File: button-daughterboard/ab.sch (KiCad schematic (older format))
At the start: 9 parts, among them J6 Conn_01x01, J7 Conn_01x01, J8 Conn_01x01, SW5 SW_Push, SW6 SW_Push

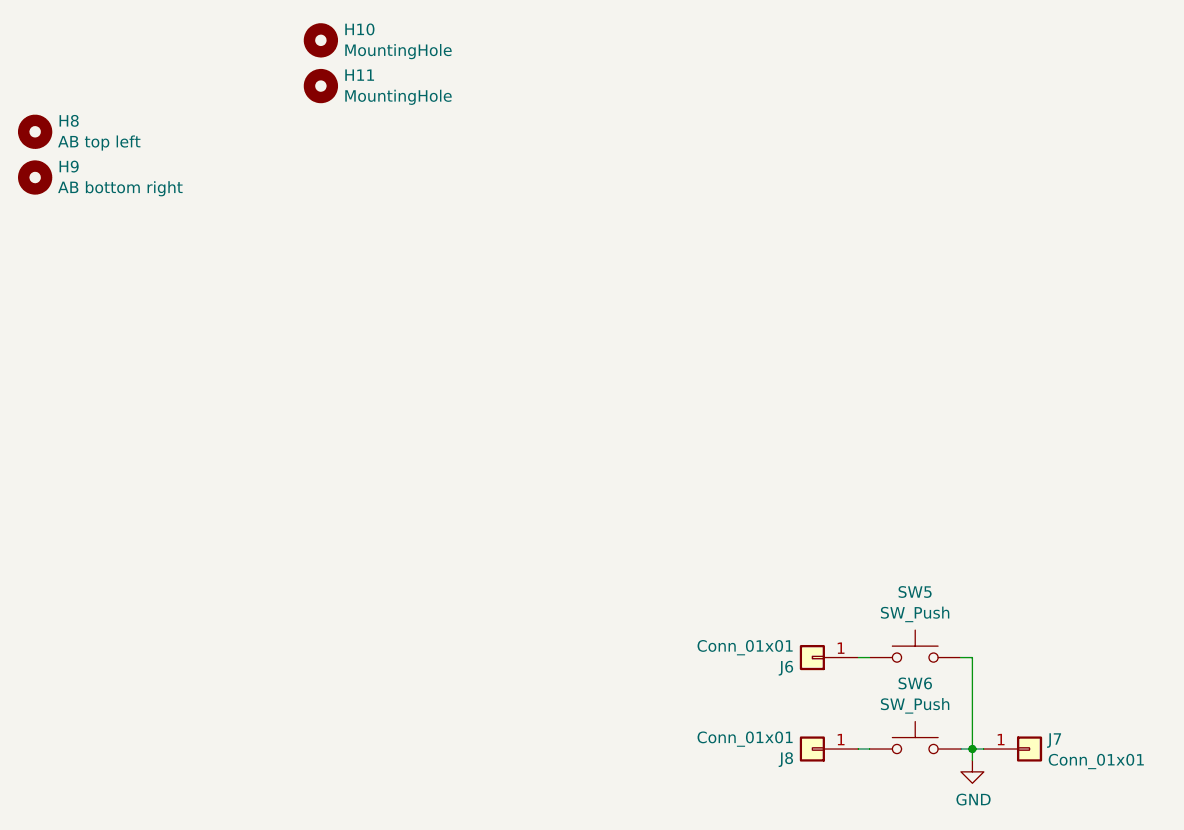
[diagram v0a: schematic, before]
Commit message: Panelize button daughterboards
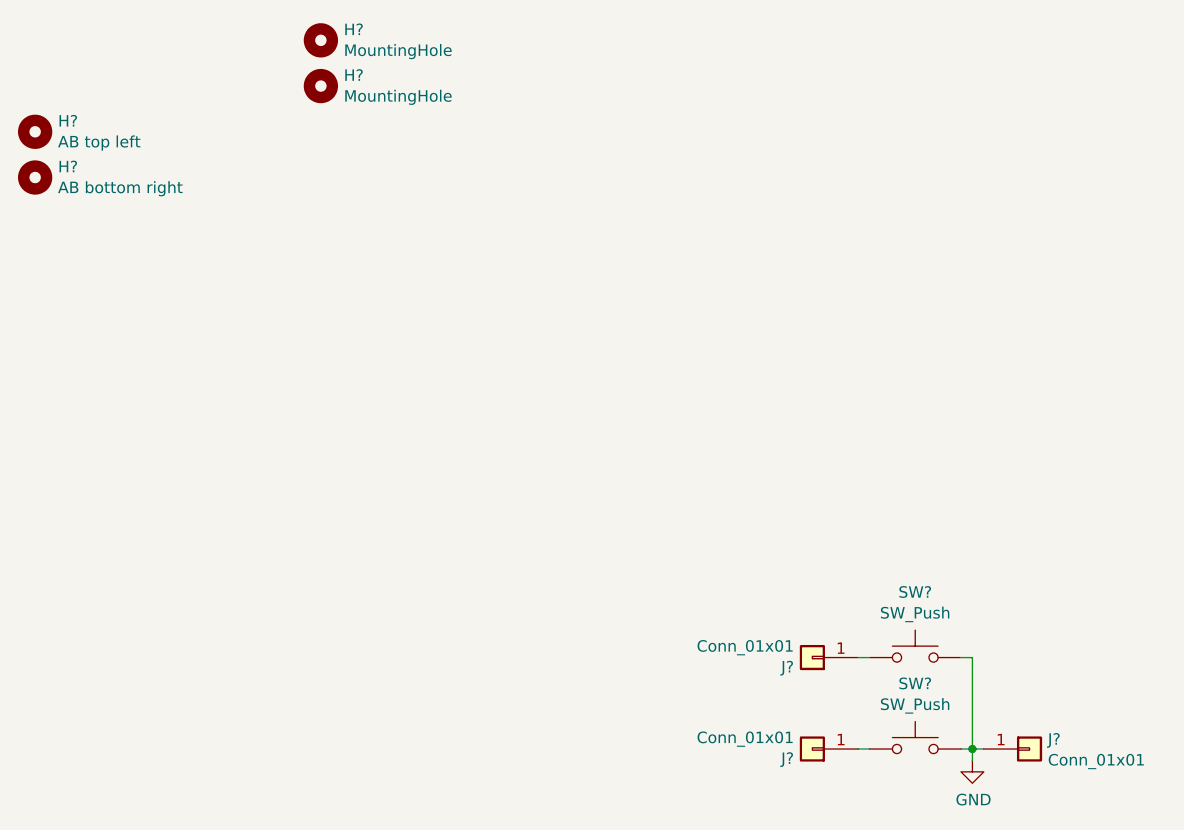
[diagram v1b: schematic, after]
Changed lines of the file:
@@
 AR Path="/60041E92/60041EAD/600661EF" Ref="#PWR?"  Part="1"
 AR Path="/60041E92/60041EBE/600661EF" Ref="#PWR0101"  Part="1"
-F 0 "#PWR0101" H 4750 3600 50  0001 C CNN
+AR Path="/60071EAD/60041EBE/600661EF" Ref="#PWR?"  Part="1"
+AR Path="/60071EBB/60041EBE/600661EF" Ref="#PWR?"  Part="1"
+F 0 "#PWR?" H 4750 3600 50  0001 C CNN
 F 1 "GND" H 4755 3677 50  0000 C CNN
 F 2 "" H 4750 3850 50  0001 C CNN
@@
 AR Path="/60041E92/60041EAD/60066206" Ref="H?"  Part="1"
 AR Path="/60041E92/60041EBE/60066206" Ref="H10"  Part="1"
-F 0 "H10" H 2000 746 50  0000 L CNN
+AR Path="/60071EAD/60041EBE/60066206" Ref="H?"  Part="1"
+AR Path="/60071EBB/60041EBE/60066206" Ref="H?"  Part="1"
+F 0 "H?" H 2000 746 50  0000 L CNN
 F 1 "MountingHole" H 2000 655 50  0000 L CNN
 F 2 "MountingHole:MountingHole_3.2mm_M3" H 1900 700 50  0001 C CNN
@@
 AR Path="/60041E92/60041EAD/6006620C" Ref="H?"  Part="1"
 AR Path="/60041E92/60041EBE/6006620C" Ref="H11"  Part="1"
-F 0 "H11" H 2000 946 50  0000 L CNN
+AR Path="/60071EAD/60041EBE/6006620C" Ref="H?"  Part="1"
+AR Path="/60071EBB/60041EBE/6006620C" Ref="H?"  Part="1"
+F 0 "H?" H 2000 946 50  0000 L CNN
 F 1 "MountingHole" H 2000 855 50  0000 L CNN
 F 2 "MountingHole:MountingHole_3.2mm_M3" H 1900 900 50  0001 C CNN
@@
 AR Path="/60041E92/60041EAD/6006621E" Ref="H?"  Part="1"
 AR Path="/60041E92/60041EBE/6006621E" Ref="H8"  Part="1"
-F 0 "H8" H 750 1146 50  0000 L CNN
+AR Path="/60071EAD/60041EBE/6006621E" Ref="H?"  Part="1"
+AR Path="/60071EBB/60041EBE/6006621E" Ref="H?"  Part="1"
+F 0 "H?" H 750 1146 50  0000 L CNN
 F 1 "AB top left" H 750 1055 50  0000 L CNN
 F 2 "MountingHole:MountingHole_3.5mm" H 650 1100 50  0001 C CNN
@@
 AR Path="/60041E92/60041EAD/60066224" Ref="H?"  Part="1"
 AR Path="/60041E92/60041EBE/60066224" Ref="H9"  Part="1"
-F 0 "H9" H 750 1346 50  0000 L CNN
+AR Path="/60071EAD/60041EBE/60066224" Ref="H?"  Part="1"
+AR Path="/60071EBB/60041EBE/60066224" Ref="H?"  Part="1"
+F 0 "H?" H 750 1346 50  0000 L CNN
 F 1 "AB bottom right" H 750 1255 50  0000 L CNN
 F 2 "MountingHole_GBA:MountingHole_GBA_AB_bottom_right" H 650 1300 50  0001 C CNN
@@
 AR Path="/60041E92/60041EAD/6006622A" Ref="J?"  Part="1"
 AR Path="/60041E92/60041EBE/6006622A" Ref="J8"  Part="1"
-F 0 "J8" H 4130 3842 50  0000 L CNN
+AR Path="/60071EAD/60041EBE/6006622A" Ref="J?"  Part="1"
+AR Path="/60071EBB/60041EBE/6006622A" Ref="J?"  Part="1"
+F 0 "J?" H 4130 3842 50  0000 L CNN
 F 1 "Conn_01x01" H 4130 3751 50  0000 L CNN
 F 2 "Connector_PinHeader_2.54mm:PinHeader_1x01_P2.54mm_Vertical" H 4050 3800 50  0001 C CNN
@@
 AR Path="/60041E92/60041EAD/60066231" Ref="J?"  Part="1"
 AR Path="/60041E92/60041EBE/60066231" Ref="J7"  Part="1"
-F 0 "J7" H 5080 3842 50  0000 L CNN
+AR Path="/60071EAD/60041EBE/60066231" Ref="J?"  Part="1"
+AR Path="/60071EBB/60041EBE/60066231" Ref="J?"  Part="1"
+F 0 "J?" H 5080 3842 50  0000 L CNN
 F 1 "Conn_01x01" H 5080 3751 50  0000 L CNN
 F 2 "Connector_PinHeader_2.54mm:PinHeader_1x01_P2.54mm_Vertical" H 5000 3800 50  0001 C CNN
@@
 AR Path="/60041E92/60041EAD/60066238" Ref="J?"  Part="1"
 AR Path="/60041E92/60041EBE/60066238" Ref="J6"  Part="1"
-F 0 "J6" H 4130 3442 50  0000 L CNN
+AR Path="/60071EAD/60041EBE/60066238" Ref="J?"  Part="1"
+AR Path="/60071EBB/60041EBE/60066238" Ref="J?"  Part="1"
+F 0 "J?" H 4130 3442 50  0000 L CNN
 F 1 "Conn_01x01" H 4130 3351 50  0000 L CNN
 F 2 "Connector_PinHeader_2.54mm:PinHeader_1x01_P2.54mm_Vertical" H 4050 3400 50  0001 C CNN
@@
 AR Path="/60041E92/60041EAD/60066253" Ref="SW?"  Part="1"
 AR Path="/60041E92/60041EBE/60066253" Ref="SW5"  Part="1"
-F 0 "SW5" H 4500 3685 50  0000 C CNN
+AR Path="/60071EAD/60041EBE/60066253" Ref="SW?"  Part="1"
+AR Path="/60071EBB/60041EBE/60066253" Ref="SW?"  Part="1"
+F 0 "SW?" H 4500 3685 50  0000 C CNN
 F 1 "SW_Push" H 4500 3594 50  0000 C CNN
 F 2 "Button_Carbon:Button_Carbon_5mm" H 4500 3600 50  0001 C CNN
@@
 AR Path="/60041E92/60041EAD/60066259" Ref="SW?"  Part="1"
 AR Path="/60041E92/60041EBE/60066259" Ref="SW6"  Part="1"
-F 0 "SW6" H 4500 4085 50  0000 C CNN
+AR Path="/60071EAD/60041EBE/60066259" Ref="SW?"  Part="1"
+AR Path="/60071EBB/60041EBE/60066259" Ref="SW?"  Part="1"
+F 0 "SW?" H 4500 4085 50  0000 C CNN
 F 1 "SW_Push" H 4500 3994 50  0000 C CNN
 F 2 "Button_Carbon:Button_Carbon_5mm" H 4500 4000 50  0001 C CNN
